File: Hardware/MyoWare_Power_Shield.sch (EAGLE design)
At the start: 11 parts

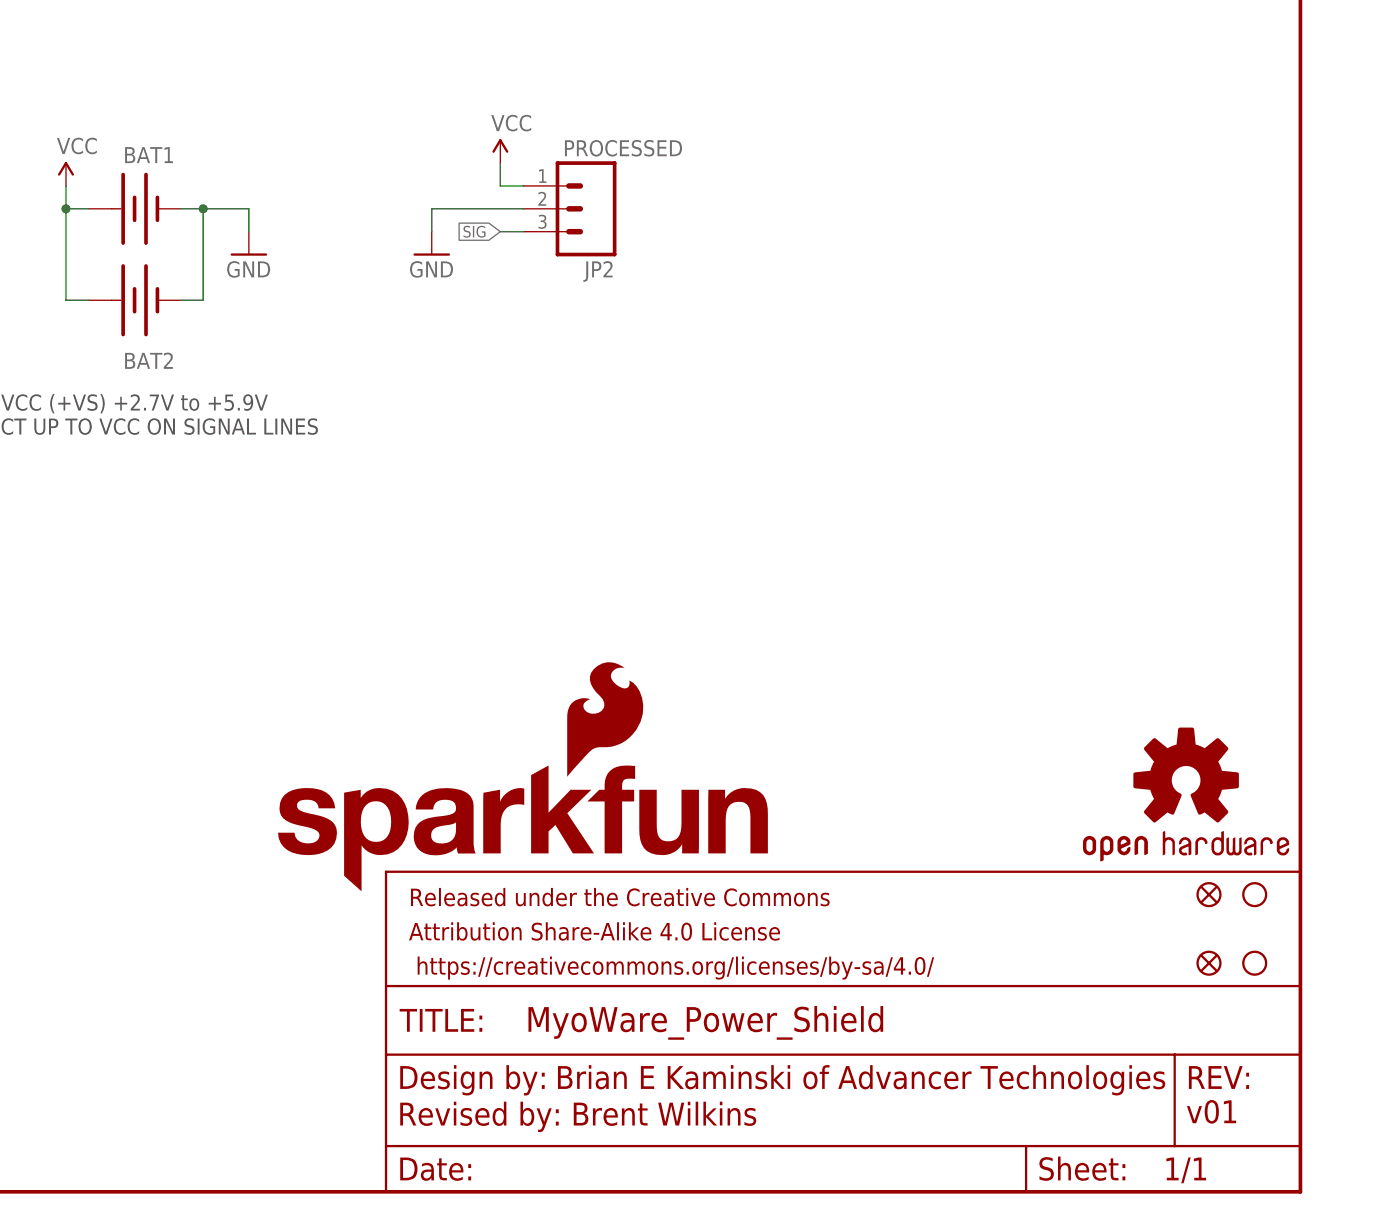
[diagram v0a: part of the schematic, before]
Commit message: Changed to standard paste version of battery holder
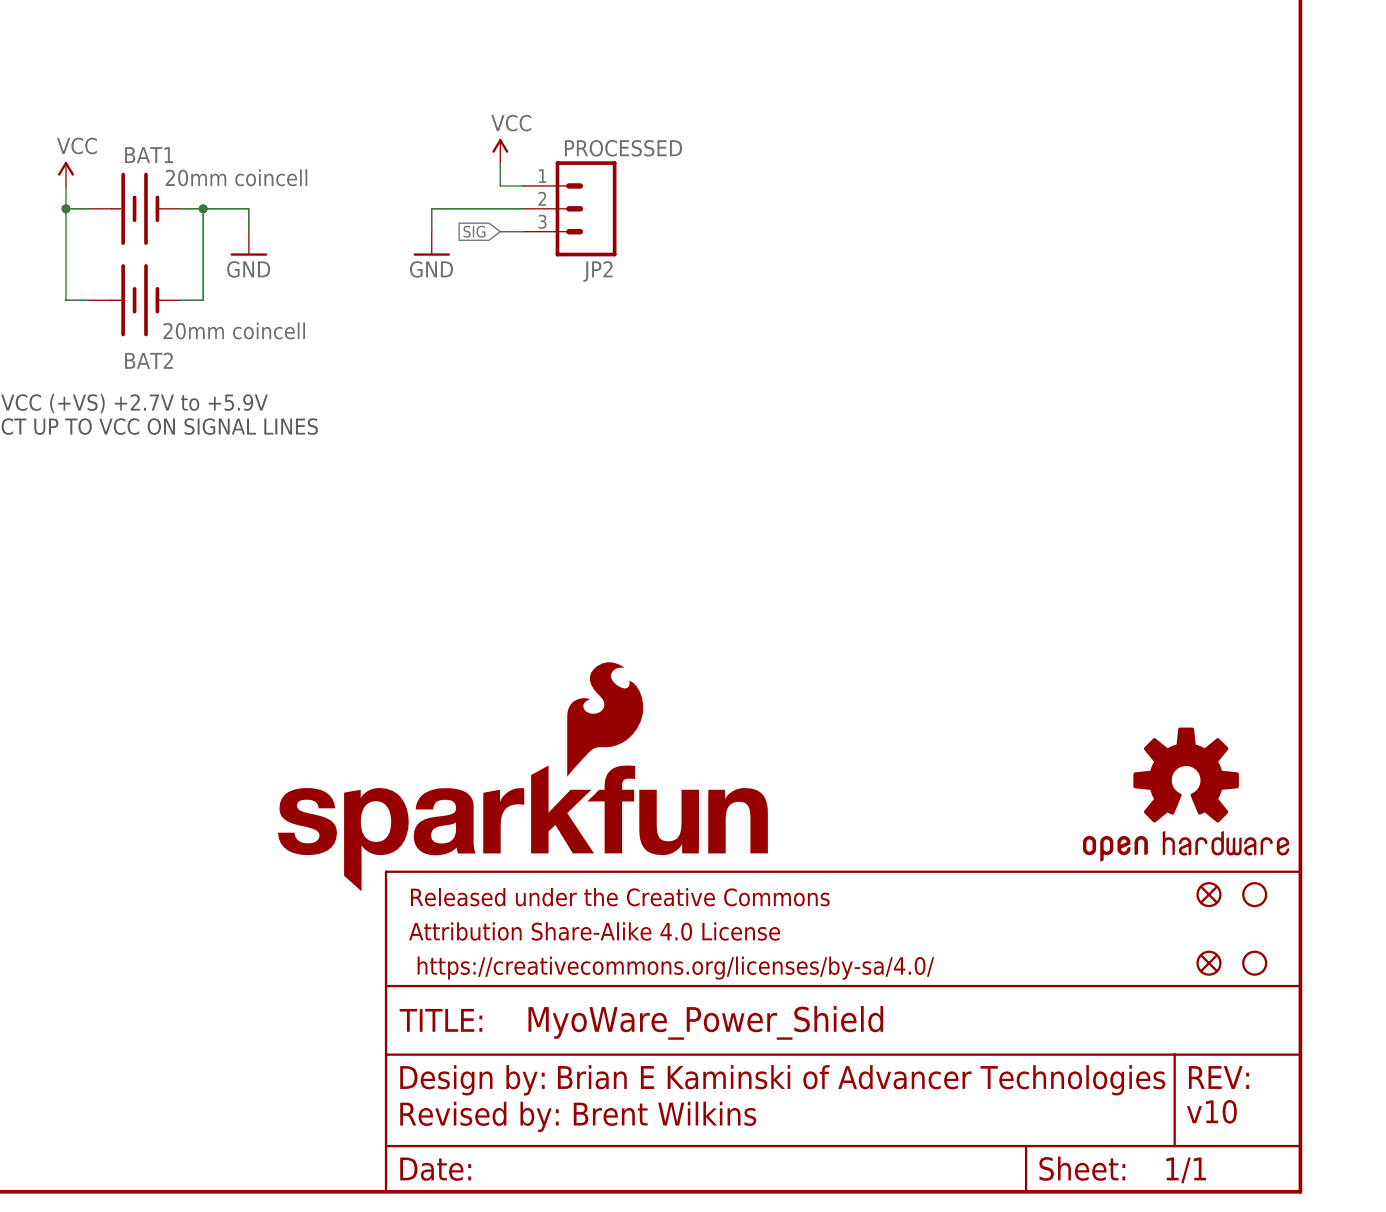
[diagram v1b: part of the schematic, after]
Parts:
- BAT1, BAT2: value (none) -> 20mm coincell; device SparkFun-Electromechanical:BATTERY20MM_4LEGS_OVERPASTE -> SparkFun-Electromechanical:BATTERY20MM_4LEGS
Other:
- note added: "v10"
- note removed: "v01"
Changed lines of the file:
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@@
 <?xml version="1.0" encoding="utf-8"?>
 <!DOCTYPE eagle SYSTEM "eagle.dtd">
-<eagle version="7.3.1">
+<eagle version="7.3.0">
 <drawing>
 <settings>
@@
 <part name="JP3" library="SparkFunJan2012" deviceset="STAND-OFF" device=""/>
 <part name="JP4" library="SparkFunJan2012" deviceset="STAND-OFF" device=""/>
-<part name="BAT1" library="SparkFun-Electromechanical" deviceset="BATTERY" device="20MM_4LEGS_OVERPASTE">
+<part name="BAT1" library="SparkFun-Electromechanical" deviceset="BATTERY" device="20MM_4LEGS" value="20mm coincell">
 <attribute name="PROD_ID" value="BATT-10373"/>
 </part>
-<part name="BAT2" library="SparkFun-Electromechanical" deviceset="BATTERY" device="20MM_4LEGS_OVERPASTE">
+<part name="BAT2" library="SparkFun-Electromechanical" deviceset="BATTERY" device="20MM_4LEGS" value="20mm coincell">
 <attribute name="PROD_ID" value="BATT-10373"/>
 </part>
@@
 <text x="308.356" y="-46.99" size="2.54" layer="94">Brian E Kaminski of Advancer Technologies</text>
 <text x="290.83" y="-51.054" size="2.54" layer="94" ratio="10">Revised by: Brent Wilkins</text>
-<text x="378.46" y="-50.8" size="2.54" layer="94" font="vector">v01</text>
+<text x="378.46" y="-50.8" size="2.54" layer="94" font="vector">v10</text>
 <text x="261.62" y="27.94" size="1.778" layer="97" font="vector" ratio="15" align="center">VCC (+VS) +2.7V to +5.9V
 EXPECT UP TO VCC ON SIGNAL LINES</text>
@@
 <attribute name="PROD_ID" x="261.62" y="50.8" size="1.778" layer="96" display="off"/>
 <attribute name="NAME" x="260.35" y="55.88" size="1.778" layer="95"/>
-<attribute name="VALUE" x="257.81" y="44.45" size="1.778" layer="96"/>
+<attribute name="VALUE" x="264.922" y="53.34" size="1.778" layer="96"/>
 </instance>
 <instance part="BAT2" gate="G$1" x="261.62" y="40.64" smashed="yes">
 <attribute name="PROD_ID" x="261.62" y="40.64" size="1.778" layer="96" display="off"/>
 <attribute name="NAME" x="260.35" y="33.02" size="1.778" layer="95"/>
-<attribute name="VALUE" x="257.81" y="34.29" size="1.778" layer="96"/>
+<attribute name="VALUE" x="264.668" y="36.322" size="1.778" layer="96"/>
 </instance>
 <instance part="JP1" gate="G$1" x="210.82" y="50.8"/>
